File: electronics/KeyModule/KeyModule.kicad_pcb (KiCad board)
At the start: 2 copper layers, 16.5 x 100 mm, 18 parts, among them SW1 SW_Push, SW2 SW_Push, SW3 SW_Push, SW4 SW_Push, SW5 SW_Push, U1 74HC165

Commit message: Keep passives out of the switch bodies; show switches in 3D
C1 and R5 sat inside a choc body's 14 mm square, where the housing
rests flat on the board. C1 moves next to U1 in the SW3/SW2 gap, R5 to
the SW5/SW4 gap, R4 onto its own lane in the SW4/SW3 gap. The switch
footprint gains a front courtyard so DRC catches this from now on, and
the kailh_choc model so the 3D view shows the fit. Three more GND
stitching vias join fill islands the front tracks had cut off.

Co-Authored-By: Claude Fable 5.1 <noreply@anthropic.com>
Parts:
- moved R4 18.8 mm to (72.3, 81.0), turned to 90 degrees
- moved C1 5.30 mm to (76.2, 99.4)
- moved R5 1.50 mm to (83.6, 60.0)
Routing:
- net +3.3V: track 109.1 -> 111.7 mm
- net Net-(U1-D4): track 61.5 -> 60.1 mm
- net GND: vias 5 -> 9

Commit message: Switch the interconnect to hanxia HX PM2.54/PZ2.54 horizontal headers
Same 8.5 x 2.5 mm socket body, 2.5 mm header body, 0.64 mm square
6 mm pins and 1.25 mm pin axis as the Harwin M20 pair, and their
recommended pads land inside the existing footprints, so the board is
unchanged. LCSC stocks both at a few cents; the Harwin header was out
of stock and the pair cost ten dollars a column.

Co-Authored-By: Claude Fable 5.1 <noreply@anthropic.com>
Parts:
- J_LEFT1, J_LEFT2, J_LEFT3: value M20-7910342R -> HX PM2.54-1x3P WT
- J_RIGHT1, J_RIGHT2, J_RIGHT3: value M20-8890345R -> HX PZ2.54-1x3P WT
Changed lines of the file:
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@@
 			)
 		)
-		(property "Value" "M20-8890345R"
+		(property "Value" "HX PZ2.54-1x3P WT"
 			(at 0 10.95 270)
 			(unlocked yes)
@@
 			)
 		)
-		(property "Ideal Part Number" "M20-8890345R"
-			(at 0 0 270)
-			(layer "B.Fab")
-			(hide yes)
-			(effects
-				(font
-					(size 0.5 0.5)
-					(thickness 0.1)
-				)
-				(justify mirror)
-			)
-		)
-		(property "Order Link" "https://www.digikey.com/en/products/detail/harwin-inc/M20-8890345R/6565723"
-			(at 0 0 270)
-			(layer "B.Fab")
-			(hide yes)
-			(effects
-				(font
-					(size 0.5 0.5)
-					(thickness 0.1)
-				)
-				(justify mirror)
-			)
-		)
-		(property "Vendor" "DigiKey"
+		(property "Ideal Part Number" "HX PZ2.54-1x3P WT"
+			(at 0 0 270)
+			(layer "B.Fab")
+			(hide yes)
+			(effects
+				(font
+					(size 0.5 0.5)
+					(thickness 0.1)
+				)
+				(justify mirror)
+			)
+		)
+		(property "Order Link" "https://www.lcsc.com/product-detail/C46061676.html"
+			(at 0 0 270)
+			(layer "B.Fab")
+			(hide yes)
+			(effects
+				(font
+					(size 0.5 0.5)
+					(thickness 0.1)
+				)
+				(justify mirror)
+			)
+		)
+		(property "Vendor" "LCSC"
 			(at 0 0 270)
 			(layer "B.Fab")
@@
 		)
 		(property ki_fp_filters "Connector*:*_1x??_*")
-		(property "LCSC Part #" ""
+		(property "LCSC Part #" "C46061676"
 			(at 0 0 0)
 			(layer "F.Fab")
@@
 			)
 		)
-		(property "Value" "M20-7910342R"
+		(property "Value" "HX PM2.54-1x3P WT"
 			(at 0 12 90)
 			(unlocked yes)
@@
 			)
 		)
-		(property "Ideal Part Number" "M20-7910342R"
-			(at 0 0 270)
-			(layer "B.Fab")
-			(hide yes)
-			(effects
-				(font
-					(size 0.5 0.5)
-					(thickness 0.1)
-				)
-				(justify mirror)
-			)
-		)
-		(property "Order Link" "https://jlcpcb.com/partdetail/Harwin-M207910342R/C3321821"
+		(property "Ideal Part Number" "HX PM2.54-1x3P WT"
+			(at 0 0 270)
+			(layer "B.Fab")
+			(hide yes)
+			(effects
+				(font
+					(size 0.5 0.5)
+					(thickness 0.1)
+				)
+				(justify mirror)
+			)
+		)
+		(property "Order Link" "https://www.lcsc.com/product-detail/C46061767.html"
 			(at 0 0 270)
 			(layer "B.Fab")
@@
 		)
 		(property ki_fp_filters "Connector*:*_1x??_*")
-		(property "LCSC Part #" "C3321821"
+		(property "LCSC Part #" "C46061767"
 			(at 0 0 0)
 			(layer "F.Fab")
@@
 			)
 		)
-		(property "Value" "M20-7910342R"
+		(property "Value" "HX PM2.54-1x3P WT"
 			(at 0 12 90)
 			(unlocked yes)
@@
 			)
 		)
-		(property "Ideal Part Number" "M20-7910342R"
-			(at 0 0 270)
-			(layer "B.Fab")
-			(hide yes)
-			(effects
-				(font
-					(size 0.5 0.5)
-					(thickness 0.1)
-				)
-				(justify mirror)
-			)
-		)
-		(property "Order Link" "https://jlcpcb.com/partdetail/Harwin-M207910342R/C3321821"
+		(property "Ideal Part Number" "HX PM2.54-1x3P WT"
+			(at 0 0 270)
+			(layer "B.Fab")
+			(hide yes)
+			(effects
+				(font
+					(size 0.5 0.5)
+					(thickness 0.1)
+				)
+				(justify mirror)
+			)
+		)
+		(property "Order Link" "https://www.lcsc.com/product-detail/C46061767.html"
 			(at 0 0 270)
 			(layer "B.Fab")
@@
 		)
 		(property ki_fp_filters "Connector*:*_1x??_*")
-		(property "LCSC Part #" "C3321821"
+		(property "LCSC Part #" "C46061767"
 			(at 0 0 0)
 			(layer "F.Fab")
@@
 			)
 		)
-		(property "Value" "M20-7910342R"
+		(property "Value" "HX PM2.54-1x3P WT"
 			(at 0 12 90)
 			(unlocked yes)
@@
 			)
 		)
-		(property "Ideal Part Number" "M20-7910342R"
-			(at 0 0 270)
-			(layer "B.Fab")
-			(hide yes)
-			(effects
-				(font
-					(size 0.5 0.5)
-					(thickness 0.1)
-				)
-				(justify mirror)
-			)
-		)
-		(property "Order Link" "https://jlcpcb.com/partdetail/Harwin-M207910342R/C3321821"
+		(property "Ideal Part Number" "HX PM2.54-1x3P WT"
+			(at 0 0 270)
+			(layer "B.Fab")
+			(hide yes)
+			(effects
+				(font
+					(size 0.5 0.5)
+					(thickness 0.1)
+				)
+				(justify mirror)
+			)
+		)
+		(property "Order Link" "https://www.lcsc.com/product-detail/C46061767.html"
 			(at 0 0 270)
 			(layer "B.Fab")
@@
 		)
 		(property ki_fp_filters "Connector*:*_1x??_*")
-		(property "LCSC Part #" "C3321821"
+		(property "LCSC Part #" "C46061767"
 			(at 0 0 0)
 			(layer "F.Fab")
@@
 			)
 		)
-		(property "Value" "M20-8890345R"
+		(property "Value" "HX PZ2.54-1x3P WT"
 			(at 0 10.95 270)
 			(unlocked yes)
@@
 			)
 		)
-		(property "Ideal Part Number" "M20-8890345R"
-			(at 0 0 270)
-			(layer "B.Fab")
-			(hide yes)
-			(effects
-				(font
-					(size 0.5 0.5)
-					(thickness 0.1)
-				)
-				(justify mirror)
-			)
-		)
-		(property "Order Link" "https://www.digikey.com/en/products/detail/harwin-inc/M20-8890345R/6565723"
-			(at 0 0 270)
-			(layer "B.Fab")
-			(hide yes)
-			(effects
-				(font
-					(size 0.5 0.5)
-					(thickness 0.1)
-				)
-				(justify mirror)
-			)
-		)
-		(property "Vendor" "DigiKey"
+		(property "Ideal Part Number" "HX PZ2.54-1x3P WT"
+			(at 0 0 270)
+			(layer "B.Fab")
+			(hide yes)
+			(effects
+				(font
+					(size 0.5 0.5)
+					(thickness 0.1)
+				)
+				(justify mirror)
+			)
+		)
+		(property "Order Link" "https://www.lcsc.com/product-detail/C46061676.html"
+			(at 0 0 270)
+			(layer "B.Fab")
+			(hide yes)
+			(effects
+				(font
+					(size 0.5 0.5)
+					(thickness 0.1)
+				)
+				(justify mirror)
+			)
+		)
+		(property "Vendor" "LCSC"
 			(at 0 0 270)
 			(layer "B.Fab")
@@
 		)
 		(property ki_fp_filters "Connector*:*_1x??_*")
-		(property "LCSC Part #" ""
+		(property "LCSC Part #" "C46061676"
 			(at 0 0 0)
 			(layer "F.Fab")
@@
 			)
 		)
-		(property "Value" "M20-8890345R"
+		(property "Value" "HX PZ2.54-1x3P WT"
 			(at 0 10.95 270)
 			(unlocked yes)
@@
 			)
 		)
-		(property "Ideal Part Number" "M20-8890345R"
-			(at 0 0 270)
-			(layer "B.Fab")
-			(hide yes)
-			(effects
-				(font
-					(size 0.5 0.5)
-					(thickness 0.1)
-				)
-				(justify mirror)
-			)
-		)
-		(property "Order Link" "https://www.digikey.com/en/products/detail/harwin-inc/M20-8890345R/6565723"
-			(at 0 0 270)
-			(layer "B.Fab")
-			(hide yes)
-			(effects
-				(font
-					(size 0.5 0.5)
-					(thickness 0.1)
-				)
-				(justify mirror)
-			)
-		)
-		(property "Vendor" "DigiKey"
+		(property "Ideal Part Number" "HX PZ2.54-1x3P WT"
+			(at 0 0 270)
+			(layer "B.Fab")
+			(hide yes)
+			(effects
+				(font
+					(size 0.5 0.5)
+					(thickness 0.1)
+				)
+				(justify mirror)
+			)
+		)
+		(property "Order Link" "https://www.lcsc.com/product-detail/C46061676.html"
+			(at 0 0 270)
+			(layer "B.Fab")
+			(hide yes)
+			(effects
+				(font
+					(size 0.5 0.5)
+					(thickness 0.1)
+				)
+				(justify mirror)
+			)
+		)
+		(property "Vendor" "LCSC"
 			(at 0 0 270)
 			(layer "B.Fab")
@@
 		)
 		(property ki_fp_filters "Connector*:*_1x??_*")
-		(property "LCSC Part #" ""
+		(property "LCSC Part #" "C46061676"
 			(at 0 0 0)
 			(layer "F.Fab")

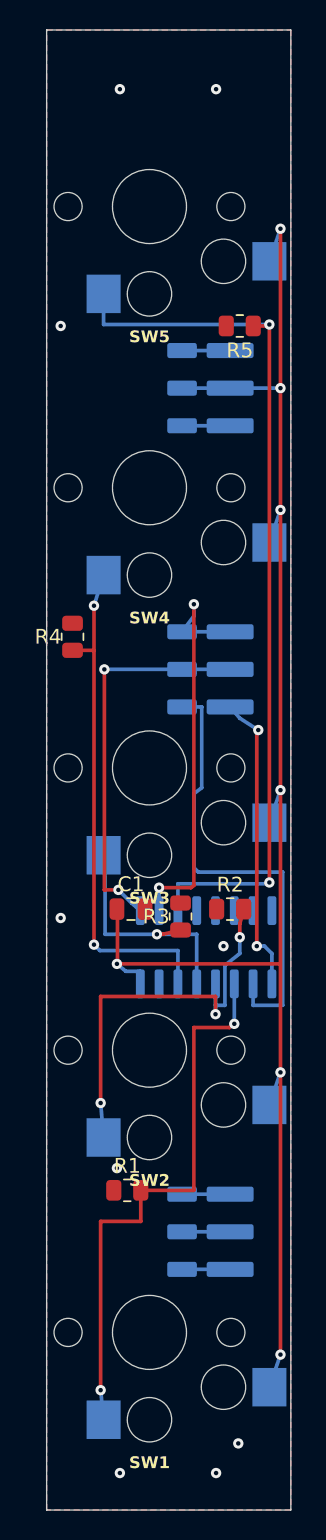
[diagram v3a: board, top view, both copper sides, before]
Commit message: Rev 2 key module: switch footprint in the right handedness, rerouted
Own Choc v1 hotswap footprint from the Kailh drawing, socket above each
key, board 16.85 mm wide, connector rows and U1 moved into the new gaps,
fully rerouted. DRC, ERC and schematic parity clean. Fab files and BOM
regenerated; plan doc records where the layout deviates from the plan.

Co-Authored-By: Claude Fable 5.1 <noreply@anthropic.com>
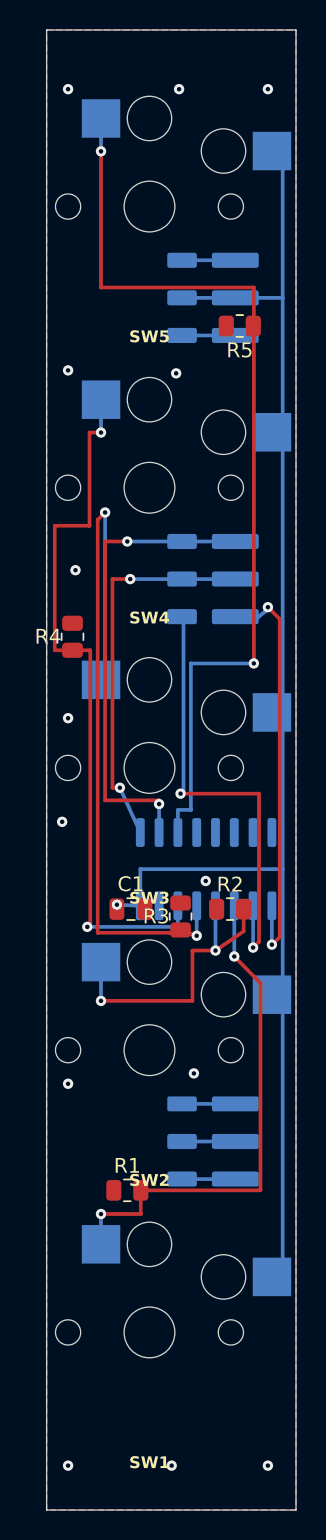
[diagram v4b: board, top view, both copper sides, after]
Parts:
- SW1, SW2, SW3, SW4, SW5: footprint kbd:keyswitch_choc12_hotswap_1u -> Library:Kailh_choc_v1_hotswap
- moved J_RIGHT2 6.11 mm to (83.3, 77.1)
- moved J_RIGHT3 6.11 mm to (83.3, 115.1)
- moved J_RIGHT1 6.11 mm to (83.3, 58.1)
- moved J_LEFT2 6.10 mm to (79.7, 77.1)
- moved J_LEFT3 6.10 mm to (79.7, 115.1)
- moved J_LEFT1 6.10 mm to (79.7, 58.1)
- moved U1 5.27 mm to (81.3, 96.7)
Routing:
- net Net-(U1-D2): track 16.5 -> 49.0 mm, vias 1 -> 2
- net +3.3V: track 111.7 -> 96.8 mm, vias 7 -> 1
- net Net-(U1-D3): track 34.6 -> 48.8 mm
- net /DATA_OUT: track 20.4 -> 28.5 mm
- net Net-(U1-D1): track 28.2 -> 20.6 mm, vias 3 -> 2
- net Net-(U1-D0): track 38.3 -> 34.4 mm
- net /CLK: track 28.3 -> 32.1 mm
- net Net-(U1-D4): track 60.1 -> 63.8 mm
- net GND: track 3.25 -> 3.60 mm, vias 9 -> 14
- net /DATA_IN: track 31.0 -> 30.8 mm, vias 0 -> 2
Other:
- board size 16.5 x 100 mm -> 16.9 x 100 mm

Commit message: Fab files carry a revision: v4
Title block, back silkscreen and file names all say v4; Electronics.md
keeps the revision table.

Co-Authored-By: Claude Fable 5.1 <noreply@anthropic.com>
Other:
- board text added: "roamyboard key v4"
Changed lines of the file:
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@@
 	)
 	(paper "A4")
+	(title_block
+		(title "roamyboard key module")
+		(rev "v4")
+		(company "nevyn.dev")
+	)
 	(layers
 		(0 "F.Cu" signal)
@@
 		(layer "Edge.Cuts")
 	)
+	(gr_text "roamyboard key v4"
+		(at 79 133.5 0)
+		(layer "B.SilkS")
+		(effects
+			(font
+				(size 1 1)
+				(thickness 0.15)
+			)
+			(justify mirror)
+		)
+	)
 	(via

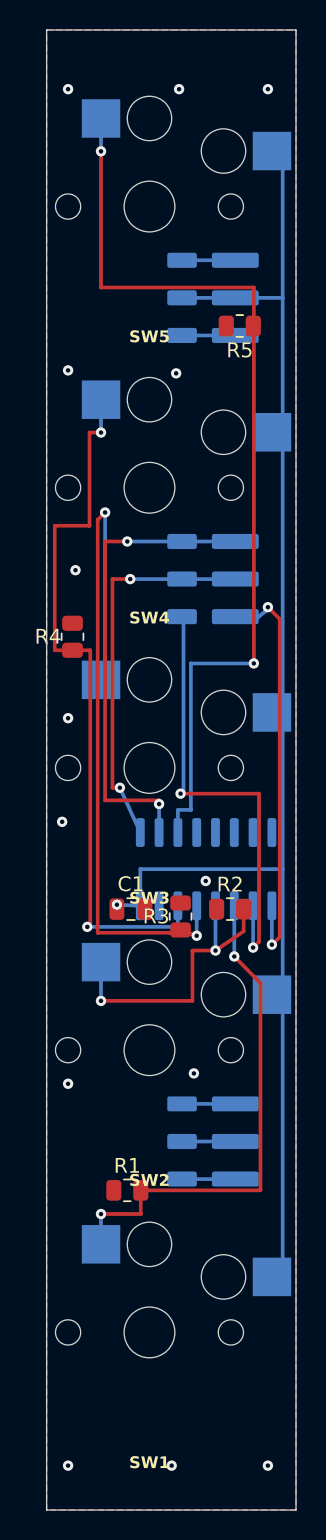
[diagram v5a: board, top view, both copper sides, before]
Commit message: v5: peg holes 1.9 mm, contact holes at the Kailh drawing's positions
The review before upload found daprice's 1.7018 mm peg holes against a
1.80 mm peg. Electronics.md prose now names bus signals by row and pin
like its own table.

Co-Authored-By: Claude Fable 5.1 <noreply@anthropic.com>
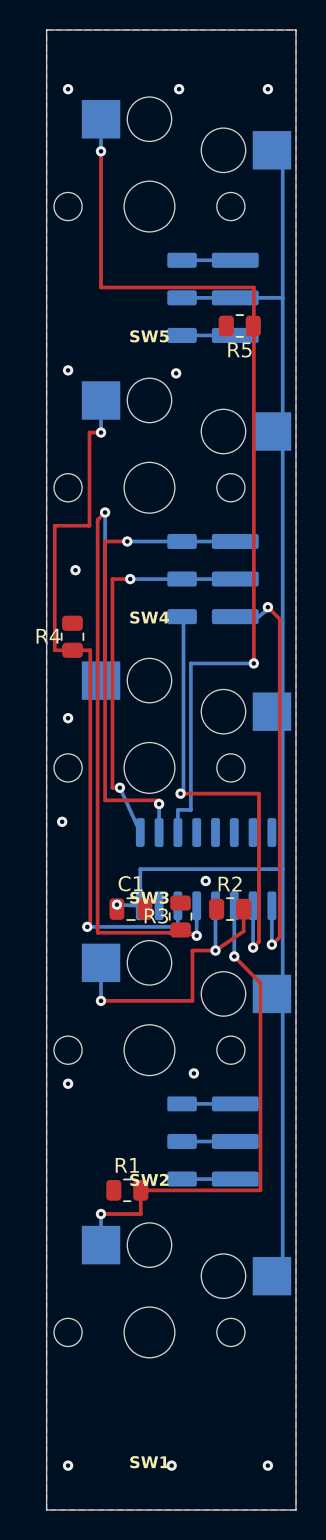
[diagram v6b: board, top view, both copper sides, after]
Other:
- board text added: "roamyboard key v5"
- board text removed: "roamyboard key v4"
